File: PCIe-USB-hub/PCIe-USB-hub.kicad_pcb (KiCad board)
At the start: 4 copper layers, 135 parts, among them J2 USB3_A_Stacked, J3 USB3_A_Stacked, J4 USB3_A_Stacked, J5 USB3_A_Stacked, J6 USB3_A_Stacked, J7 Barrel_Jack_MountingPin, U1 ST1S10PUR, Y1 X322524MQB4SI, Y2 X322524MQB4SI, Y3 X322524MQB4SI

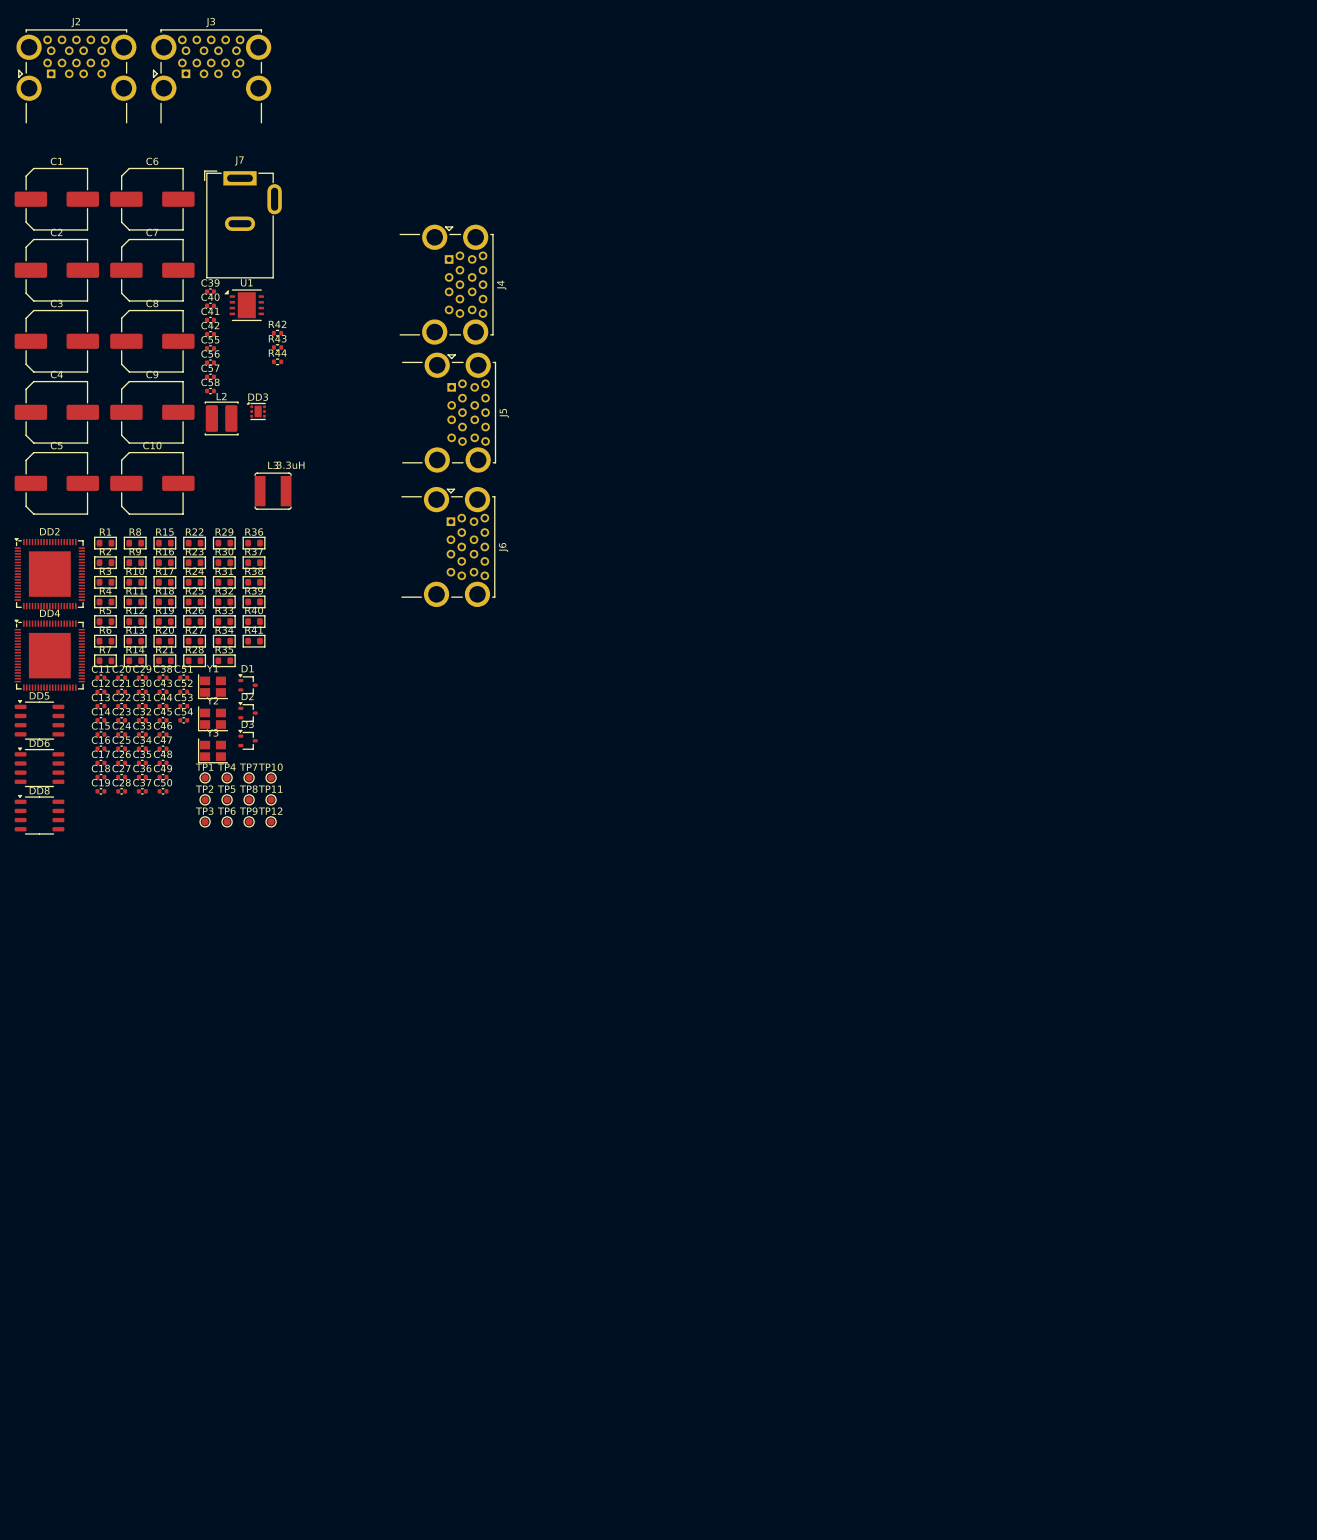
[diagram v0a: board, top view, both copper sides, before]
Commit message: Доделал схему, сделал контур платы и расстановку предварительную USB портов
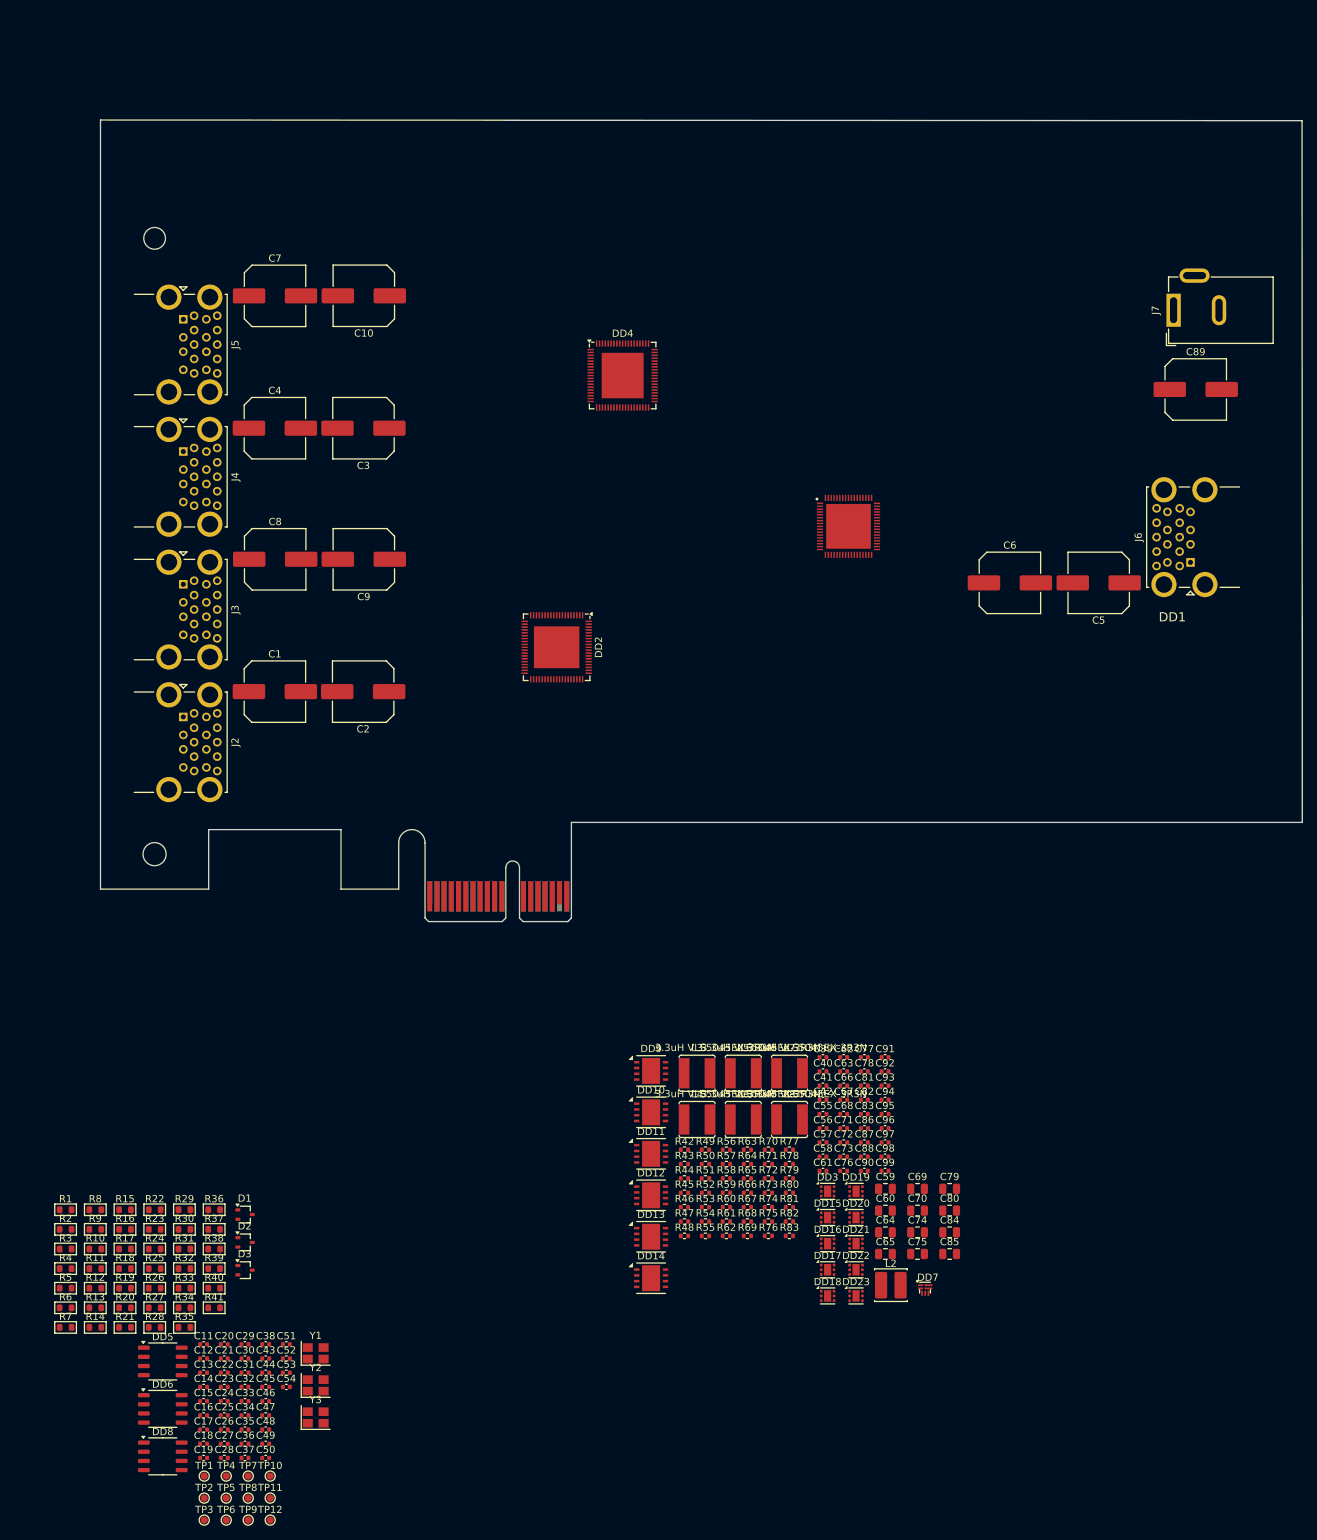
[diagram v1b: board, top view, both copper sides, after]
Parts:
- removed U1: ST1S10PUR, Package_DFN_QFN:DFN-8-1EP_4x4mm_P0.8mm_EP2.5x3.6mm
- added C59: 22uF, Capacitor_SMD:C_0805_2012Metric, F.Cu at (140.2, 175.3)
- added C60: 22uF, Capacitor_SMD:C_0805_2012Metric, F.Cu at (140.2, 178.3)
- added C61: 22uF, Capacitor_SMD:C_0402_1005Metric, F.Cu at (131.6, 172.8)
- added C62: 100nF, Capacitor_SMD:C_0402_1005Metric, F.Cu at (134.4, 157.1)
- added C63: 22uF, Capacitor_SMD:C_0402_1005Metric, F.Cu at (134.4, 159.1)
- added C64: 22uF, Capacitor_SMD:C_0805_2012Metric, F.Cu at (140.2, 181.4)
- added C65: 22uF, Capacitor_SMD:C_0805_2012Metric, F.Cu at (140.2, 184.4)
- added C66: 22uF, Capacitor_SMD:C_0402_1005Metric, F.Cu at (134.4, 161.0)
- added C67: 100nF, Capacitor_SMD:C_0402_1005Metric, F.Cu at (134.4, 163.0)
- added C68: 22uF, Capacitor_SMD:C_0402_1005Metric, F.Cu at (134.4, 165.0)
- added C69: 22uF, Capacitor_SMD:C_0805_2012Metric, F.Cu at (144.7, 175.3)
- added C70: 22uF, Capacitor_SMD:C_0805_2012Metric, F.Cu at (144.7, 178.3)
- added C71: 22uF, Capacitor_SMD:C_0402_1005Metric, F.Cu at (134.4, 166.9)
- added C72: 100nF, Capacitor_SMD:C_0402_1005Metric, F.Cu at (134.4, 168.9)
- added C73: 22uF, Capacitor_SMD:C_0402_1005Metric, F.Cu at (134.4, 170.9)
- added C74: 22uF, Capacitor_SMD:C_0805_2012Metric, F.Cu at (144.7, 181.4)
- added C75: 22uF, Capacitor_SMD:C_0805_2012Metric, F.Cu at (144.7, 184.4)
- added C76: 22uF, Capacitor_SMD:C_0402_1005Metric, F.Cu at (134.4, 172.8)
- added C77: 100nF, Capacitor_SMD:C_0402_1005Metric, F.Cu at (137.3, 157.1)
- added C78: 22uF, Capacitor_SMD:C_0402_1005Metric, F.Cu at (137.3, 159.1)
- added C79: 22uF, Capacitor_SMD:C_0805_2012Metric, F.Cu at (149.1, 175.3)
- added C80: 22uF, Capacitor_SMD:C_0805_2012Metric, F.Cu at (149.1, 178.3)
- added C81: 22uF, Capacitor_SMD:C_0402_1005Metric, F.Cu at (137.3, 161.0)
- added C82: 100nF, Capacitor_SMD:C_0402_1005Metric, F.Cu at (137.3, 163.0)
- added C83: 22uF, Capacitor_SMD:C_0402_1005Metric, F.Cu at (137.3, 165.0)
- added C84: 22uF, Capacitor_SMD:C_0805_2012Metric, F.Cu at (149.1, 181.4)
- added C85: 22uF, Capacitor_SMD:C_0805_2012Metric, F.Cu at (149.1, 184.4)
- added C86: 22uF, Capacitor_SMD:C_0402_1005Metric, F.Cu at (137.3, 166.9)
- added C87: 100nF, Capacitor_SMD:C_0402_1005Metric, F.Cu at (137.3, 168.9)
- added C88: 22uF, Capacitor_SMD:C_0402_1005Metric, F.Cu at (137.3, 170.9)
- added C89: EEEFK1E151P, Capacitor_SMD:C_Elec_8x10.2, F.Cu at (183.3, 64.5)
- added C90: 100nF, Capacitor_SMD:C_0402_1005Metric, F.Cu at (137.3, 172.8)
- added C91: 100nF, Capacitor_SMD:C_0402_1005Metric, F.Cu at (140.2, 157.1)
- added C92: 100nF, Capacitor_SMD:C_0402_1005Metric, F.Cu at (140.2, 159.1)
- added C93: 100nF, Capacitor_SMD:C_0402_1005Metric, F.Cu at (140.2, 161.0)
- added C94: 100nF, Capacitor_SMD:C_0402_1005Metric, F.Cu at (140.2, 163.0)
- added C95: 100nF, Capacitor_SMD:C_0402_1005Metric, F.Cu at (140.2, 165.0)
- added C96: 100nF, Capacitor_SMD:C_0402_1005Metric, F.Cu at (140.2, 166.9)
- added C97: 100nF, Capacitor_SMD:C_0402_1005Metric, F.Cu at (140.2, 168.9)
- added C98: 100nF, Capacitor_SMD:C_0402_1005Metric, F.Cu at (140.2, 170.9)
- added C99: 100nF, Capacitor_SMD:C_0402_1005Metric, F.Cu at (140.2, 172.8)
- added DD1: UPD720201K8-701-BAC-A, UPD720201K8:UPD720201K8, F.Cu at (135.1, 83.5)
- added DD10: ST1S10PUR, Package_DFN_QFN:DFN-8-1EP_4x4mm_P0.8mm_EP2.5x3.6mm, F.Cu at (107.7, 164.7)
- added DD11: ST1S10PUR, Package_DFN_QFN:DFN-8-1EP_4x4mm_P0.8mm_EP2.5x3.6mm, F.Cu at (107.7, 170.5)
- added DD12: ST1S10PUR, Package_DFN_QFN:DFN-8-1EP_4x4mm_P0.8mm_EP2.5x3.6mm, F.Cu at (107.7, 176.2)
- added DD13: ST1S10PUR, Package_DFN_QFN:DFN-8-1EP_4x4mm_P0.8mm_EP2.5x3.6mm, F.Cu at (107.7, 182.0)
- added DD14: ST1S10PUR, Package_DFN_QFN:DFN-8-1EP_4x4mm_P0.8mm_EP2.5x3.6mm, F.Cu at (107.7, 187.7)
- added DD15: TPS2552DRVR, Package_SON:WSON-6-1EP_2x2mm_P0.65mm_EP1x1.6mm, F.Cu at (132.2, 179.3)
- added DD16: TPS2552DRVR, Package_SON:WSON-6-1EP_2x2mm_P0.65mm_EP1x1.6mm, F.Cu at (132.2, 182.9)
- added DD17: TPS2552DRVR, Package_SON:WSON-6-1EP_2x2mm_P0.65mm_EP1x1.6mm, F.Cu at (132.2, 186.6)
- added DD18: TPS2552DRVR, Package_SON:WSON-6-1EP_2x2mm_P0.65mm_EP1x1.6mm, F.Cu at (132.2, 190.2)
- added DD19: TPS2552DRVR, Package_SON:WSON-6-1EP_2x2mm_P0.65mm_EP1x1.6mm, F.Cu at (136.2, 175.7)
- added DD20: TPS2552DRVR, Package_SON:WSON-6-1EP_2x2mm_P0.65mm_EP1x1.6mm, F.Cu at (136.2, 179.3)
- added DD21: TPS2552DRVR, Package_SON:WSON-6-1EP_2x2mm_P0.65mm_EP1x1.6mm, F.Cu at (136.2, 182.9)
- added DD22: TPS2552DRVR, Package_SON:WSON-6-1EP_2x2mm_P0.65mm_EP1x1.6mm, F.Cu at (136.2, 186.6)
- added DD23: TPS2552DRVR, Package_SON:WSON-6-1EP_2x2mm_P0.65mm_EP1x1.6mm, F.Cu at (136.2, 190.2)
- added DD7: ~, SY8843QWC:SY8843QWC, F.Cu at (145.6, 186.6)
- added DD9: ST1S10PUR, Package_DFN_QFN:DFN-8-1EP_4x4mm_P0.8mm_EP2.5x3.6mm, F.Cu at (107.7, 159.0)
- added J1: PCIexpress_x1, PCIexpress:PCIexpress_x1, F.Cu at (76.5, 138.3)
- added L4: 3.3uH VLS5045EX-3R3N, PCM_4ms_Inductor:COIL_5040, F.Cu at (114.1, 165.7)
- added L5: 3.3uH VLS5045EX-3R3N, PCM_4ms_Inductor:COIL_5040, F.Cu at (120.5, 159.3)
- added L6: 3.3uH VLS5045EX-3R3N, PCM_4ms_Inductor:COIL_5040, F.Cu at (120.5, 165.7)
- added L7: 3.3uH VLS5045EX-3R3N, PCM_4ms_Inductor:COIL_5040, F.Cu at (126.9, 159.3)
- added L8: 3.3uH VLS5045EX-3R3N, PCM_4ms_Inductor:COIL_5040, F.Cu at (126.9, 165.7)
- added R45: 0R, Resistor_SMD:R_0402_1005Metric, F.Cu at (112.4, 175.9)
- added R46: 0R, Resistor_SMD:R_0402_1005Metric, F.Cu at (112.4, 177.9)
- added R47: 4.7k, Resistor_SMD:R_0402_1005Metric, F.Cu at (112.4, 179.9)
- added R48: 1.5k, Resistor_SMD:R_0402_1005Metric, F.Cu at (112.4, 181.9)
- added R49: 0R, Resistor_SMD:R_0402_1005Metric, F.Cu at (115.3, 169.9)
- added R50: 43k, Resistor_SMD:R_0402_1005Metric, F.Cu at (115.3, 171.9)
- added R51: 8.2k, Resistor_SMD:R_0402_1005Metric, F.Cu at (115.3, 173.9)
- added R52: 0R, Resistor_SMD:R_0402_1005Metric, F.Cu at (115.3, 175.9)
- added R53: 43k, Resistor_SMD:R_0402_1005Metric, F.Cu at (115.3, 177.9)
- added R54: 8.2k, Resistor_SMD:R_0402_1005Metric, F.Cu at (115.3, 179.9)
- added R55: 0R, Resistor_SMD:R_0402_1005Metric, F.Cu at (115.3, 181.9)
- added R56: 43k, Resistor_SMD:R_0402_1005Metric, F.Cu at (118.2, 169.9)
- added R57: 8.2k, Resistor_SMD:R_0402_1005Metric, F.Cu at (118.2, 171.9)
- added R58: 0R, Resistor_SMD:R_0402_1005Metric, F.Cu at (118.2, 173.9)
- added R59: 43k, Resistor_SMD:R_0402_1005Metric, F.Cu at (118.2, 175.9)
- added R60: 8.2k, Resistor_SMD:R_0402_1005Metric, F.Cu at (118.2, 177.9)
- added R61: 0R, Resistor_SMD:R_0402_1005Metric, F.Cu at (118.2, 179.9)
- added R62: 43k, Resistor_SMD:R_0402_1005Metric, F.Cu at (118.2, 181.9)
- added R63: 8.2k, Resistor_SMD:R_0402_1005Metric, F.Cu at (121.1, 169.9)
- added R64: 100k, Resistor_SMD:R_0402_1005Metric, F.Cu at (121.1, 171.9)
- added R65: 20k, Resistor_SMD:R_0402_1005Metric, F.Cu at (121.1, 173.9)
- added R66: 100k, Resistor_SMD:R_0402_1005Metric, F.Cu at (121.1, 175.9)
- added R67: 20k, Resistor_SMD:R_0402_1005Metric, F.Cu at (121.1, 177.9)
- added R68: 100k, Resistor_SMD:R_0402_1005Metric, F.Cu at (121.1, 179.9)
- added R69: 100k, Resistor_SMD:R_0402_1005Metric, F.Cu at (121.1, 181.9)
- added R70: 20k, Resistor_SMD:R_0402_1005Metric, F.Cu at (124.0, 169.9)
- added R71: 20k, Resistor_SMD:R_0402_1005Metric, F.Cu at (124.0, 171.9)
- added R72: 100k, Resistor_SMD:R_0402_1005Metric, F.Cu at (124.0, 173.9)
- added R73: 100k, Resistor_SMD:R_0402_1005Metric, F.Cu at (124.0, 175.9)
- added R74: 20k, Resistor_SMD:R_0402_1005Metric, F.Cu at (124.0, 177.9)
- added R75: 20k, Resistor_SMD:R_0402_1005Metric, F.Cu at (124.0, 179.9)
- added R76: 100k, Resistor_SMD:R_0402_1005Metric, F.Cu at (124.0, 181.9)
- added R77: 100k, Resistor_SMD:R_0402_1005Metric, F.Cu at (126.9, 169.9)
- added R78: 20k, Resistor_SMD:R_0402_1005Metric, F.Cu at (126.9, 171.9)
- added R79: 20k, Resistor_SMD:R_0402_1005Metric, F.Cu at (126.9, 173.9)
- added R80: 100k, Resistor_SMD:R_0402_1005Metric, F.Cu at (126.9, 175.9)
- added R81: 100k, Resistor_SMD:R_0402_1005Metric, F.Cu at (126.9, 177.9)
- added R82: 20k, Resistor_SMD:R_0402_1005Metric, F.Cu at (126.9, 179.9)
- added R83: 20k, Resistor_SMD:R_0402_1005Metric, F.Cu at (126.9, 181.9)
- L3: value 3.3uH -> 3.3uH VLS5045EX-3R3N
- R43: value 14k -> 51.1k
- R44: value 24k -> 68k
- moved L2 151.8 mm to (141.0, 188.7)
- moved C5 145.1 mm to (169.8, 91.3), turned to 180 degrees
- moved C39 136.0 mm to (131.6, 157.1)
- moved C40 136.0 mm to (131.6, 159.1)
- moved C41 136.0 mm to (131.6, 161.0)
- moved C42 136.0 mm to (131.6, 163.0)
- moved C55 136.0 mm to (131.6, 165.0)
- moved C56 136.0 mm to (131.6, 166.9)
- moved C57 136.0 mm to (131.6, 168.9)
- moved C58 136.0 mm to (131.6, 170.9)
- moved DD3 133.9 mm to (132.2, 175.7)
- moved J7 130.7 mm to (180.2, 53.5), turned to 90 degrees
- moved C6 130.3 mm to (157.5, 91.3)
- moved R44 126.5 mm to (112.4, 173.9)
- moved R43 126.5 mm to (112.4, 171.9)
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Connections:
- net 0.95V renamed 1.05V
- DD2 pad 55: OCI2B -> OCI1B
- DD2 pad 59: OCI4B -> OCI3B
- DD3 pad 1: unconnected-(DD3-OUT-Pad1) -> +5V_USB1
- DD3 pad 2: unconnected-(DD3-ILIM-Pad2) -> Net-(DD3-ILIM)
- DD3 pad 3: unconnected-(DD3-#FAULT-Pad3) -> Net-(DD3-#FAULT)
- DD3 pad 5: unconnected-(DD3-GND-Pad5) -> Earth
- DD3 pad 6: unconnected-(DD3-EN-Pad6) -> OCI1B
- DD3 pad 7: unconnected-(DD3-EP-Pad7) -> Earth
- DD4 pad 55: OCI6B -> OCI5B
- DD4 pad 59: OCI8B -> OCI7B
- J7 pad 1: unconnected-(J7-Pad1) -> +12V
- J7 pad 2: unconnected-(J7-Pad2) -> Earth
- L3 pad 1: unconnected-(L3-Pad1) -> Net-(DD9-SW)
- L3 pad 2: unconnected-(L3-Pad2) -> +3.3V_DUAL
- R22 pad 1: OCI9B -> OCI10B
- R27 pad 2: OCI2B -> OCI1B
- R29 pad 2: OCI4B -> OCI3B
- R35 pad 2: OCI6B -> OCI5B
- R37 pad 2: OCI8B -> OCI7B
- R42 pad 1: POW_95_EN -> +3.3V
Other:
- board outline added: 166.7 x 111.2 mm

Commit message: тык тык поменял разъёмы на одинарные
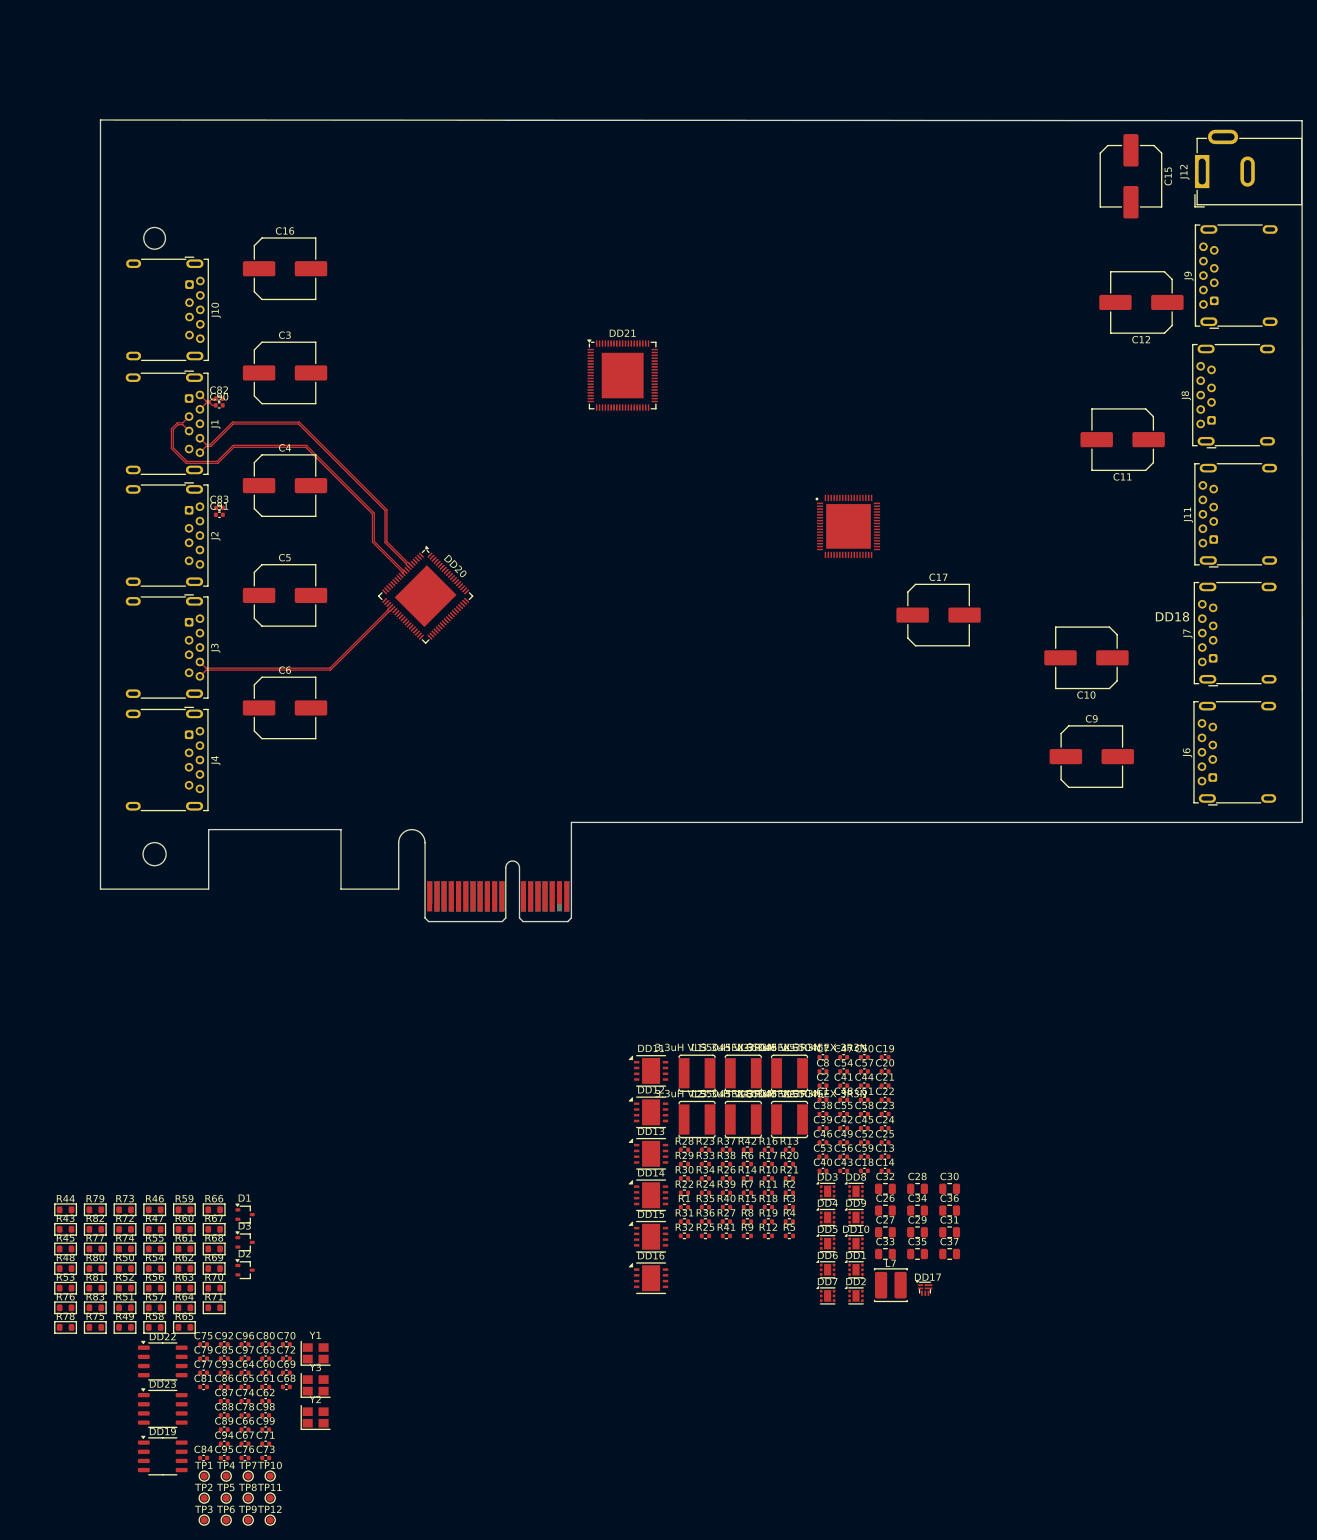
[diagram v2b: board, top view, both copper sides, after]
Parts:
- removed the J5 at (42.9, 54.8)
- added J1: USB3_A, Connector_USB:USB3_A_Molex_48393-001, F.Cu at (43.7, 65.8)
- added J10: USB3_A, Connector_USB:USB3_A_Molex_48393-001, F.Cu at (43.7, 50.0)
- added J11: USB3_A, Connector_USB:USB3_A_Molex_48393-001, F.Cu at (185.8, 85.3)
- added J7: USB3_A, Connector_USB:USB3_A_Molex_48393-001, F.Cu at (185.7, 101.8)
- added J8: USB3_A, Connector_USB:USB3_A_Molex_48393-001, F.Cu at (185.4, 68.8)
- added J9: USB3_A, Connector_USB:USB3_A_Molex_48393-001, F.Cu at (185.8, 52.2)
- J2, J3, J4, J6: value USB3_A_Stacked -> USB3_A; footprint Connector_USB:USB3_A_Molex_48406-0001_Horizontal_Stacked -> Connector_USB:USB3_A_Molex_48393-001
- moved C82 141.0 mm to (47.9, 65.8)
- moved C90 138.1 mm to (47.9, 66.7)
- moved C91 128.8 mm to (47.9, 81.9)
- moved C83 127.8 mm to (47.9, 80.9)
- moved C9 122.1 mm to (168.8, 115.4)
- moved C16 120.9 mm to (57.0, 47.8), turned to 0 degrees
- moved C11 119.2 mm to (173.1, 71.5), turned to 180 degrees
- moved C12 107.8 mm to (175.7, 52.4)
- moved C10 105.2 mm to (168.1, 101.7)
- moved C3 44.2 mm to (57.0, 62.2)
- moved J4 39.3 mm to (43.7, 112.4)
- moved C15 30.9 mm to (174.3, 34.9), turned to -90 degrees
- moved C4 30.6 mm to (57.0, 77.8), turned to 0 degrees
- moved J6 30.0 mm to (185.6, 118.3)
- moved J2 28.7 mm to (43.7, 81.2)
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- renumbered C42 to C1, C3 to C10, C7 to C11, C10 to C12, C98 to C13, C99 to C14, C89 to C15, C5 to C16, C6 to C17, C90 to C18, C91 to C19, C41 to C2, C92 to C20, C93 to C21, C94 to C22, C95 to C23, C96 to C24, C97 to C25, C60 to C26, C64 to C27, C69 to C28, C74 to C29, C1 to C3, C79 to C30, C84 to C31, C59 to C32, C65 to C33, C70 to C34, C75 to C35, C80 to C36, C85 to C37, C55 to C38, C56 to C39, C2 to C4, C61 to C40, C66 to C41, C71 to C42, C76 to C43, C81 to C44, C86 to C45, C57 to C46, C62 to C47, C67 to C48, C72 to C49, C8 to C5, C77 to C50, C82 to C51, C87 to C52, C58 to C53, C63 to C54, C68 to C55, C73 to C56, C78 to C57, C83 to C58, C88 to C59, C9 to C6, C44 to C60, C45 to C61, C46 to C62, C43 to C63, C31 to C64, C32 to C65, C35 to C66, C36 to C67, C54 to C68, C53 to C69, C39 to C7, C51 to C70, C49 to C71, C52 to C72, C50 to C73, C33 to C74, C11 to C75, C37 to C76, C13 to C77, C34 to C78, C12 to C79, C40 to C8, C38 to C80, C14 to C81, C16 to C82, C17 to C83, C19 to C84, C21 to C85, C23 to C86, C24 to C87, C25 to C88, C26 to C89, C4 to C9, C15 to C90, C18 to C91, C20 to C92, C22 to C93, C27 to C94, C28 to C95, C29 to C96, C30 to C97, C47 to C98, C48 to C99, D3 to D2, D2 to D3, DD22 to DD1, DD21 to DD10, DD9 to DD11, DD10 to DD12, DD11 to DD13, DD12 to DD14, DD13 to DD15, DD14 to DD16, DD7 to DD17, DD1 to DD18, DD8 to DD19, DD23 to DD2, DD2 to DD20, DD4 to DD21, DD5 to DD22, DD6 to DD23, DD15 to DD4, DD16 to DD5, DD17 to DD6, DD18 to DD7, DD19 to DD8, DD20 to DD9, J7 to J12, J1 to J5, L3 to L1, L4 to L2, L5 to L3, L6 to L4, L7 to L5, L8 to L6, L2 to L7, R46 to R1, R72 to R10, R73 to R11, R76 to R12, R77 to R13, R65 to R14, R67 to R15, R70 to R16, R71 to R17, R74 to R18, R75 to R19, R80 to R2, R78 to R20, R79 to R21, R45 to R22, R49 to R23, R52 to R24, R55 to R25, R58 to R26, R61 to R27, R42 to R28, R43 to R29, R81 to R3, R44 to R30, R47 to R31, R48 to R32, R50 to R33, R51 to R34, R53 to R35, R54 to R36, R56 to R37, R57 to R38, R59 to R39, R82 to R4, R60 to R40, R62 to R41, R63 to R42, R2 to R43, R1 to R44, R3 to R45, R22 to R46, R23 to R47, R4 to R48, R21 to R49, R83 to R5, R18 to R50, R20 to R51, R19 to R52, R5 to R53, R25 to R54, R24 to R55, R26 to R56, R27 to R57, R28 to R58, R29 to R59, R64 to R6, R30 to R60, R31 to R61, R32 to R62, R33 to R63, R34 to R64, R35 to R65, R36 to R66, R37 to R67, R38 to R68, R39 to R69, R66 to R7, R40 to R70, R41 to R71, R16 to R72, R15 to R73, R17 to R74, R14 to R75, R6 to R76, R10 to R77, R7 to R78, R8 to R79, R68 to R8, R11 to R80, R12 to R81, R9 to R82, R13 to R83, R69 to R9, Y3 to Y2, Y2 to Y3
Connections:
- DD1 pad 4: (no net) -> PPON9
- DD10 pad 4: (no net) -> PPON8
- DD2 pad 4: (no net) -> PPON10
- DD3 pad 4: (no net) -> PPON1
- DD4 pad 4: (no net) -> PPON2
- DD5 pad 4: (no net) -> PPON3
- DD6 pad 4: (no net) -> PPON4
- DD7 pad 4: (no net) -> PPON5
- DD8 pad 4: (no net) -> PPON6
- DD9 pad 4: (no net) -> PPON7
- J2 pad 1: +5V_USB1 -> +5V_USB2
- J2 pad 10: +5V_USB2 -> Earth
- J2 pad 2: USB-downstream1-D- -> USB-downstream2-D-
- J2 pad 3: USB-downstream1-D+ -> USB-downstream2-D+
- J2 pad 5: USB-downstream1-RX- -> USB-downstream2-RX-
- J2 pad 6: USB-downstream1-RX+ -> USB-downstream2-RX+
- J2 pad 8: USB-downstream1-TX- -> USB-downstream2-TX-
- J2 pad 9: USB-downstream1-TX+ -> USB-downstream2-TX+
- J3 pad 10: +5V_USB4 -> Earth
- J4 pad 1: +5V_USB5 -> +5V_USB4
- J4 pad 10: +5V_USB6 -> Earth
- J4 pad 2: USB-downstream5-D- -> USB-downstream4-D-
- J4 pad 3: USB-downstream5-D+ -> USB-downstream4-D+
- J4 pad 5: USB-downstream5-RX- -> USB-downstream4-RX-
- J4 pad 6: USB-downstream5-RX+ -> USB-downstream4-RX+
- J4 pad 8: USB-downstream5-TX- -> USB-downstream4-TX-
- J4 pad 9: USB-downstream5-TX+ -> USB-downstream4-TX+
- J6 pad 1: +5V_USB9 -> +5V_USB5
- J6 pad 10: +5V_USB10 -> Earth
- J6 pad 2: USB-downstream9-D- -> USB-downstream5-D-
- J6 pad 3: USB-downstream9-D+ -> USB-downstream5-D+
- J6 pad 5: USB-downstream9-RX- -> USB-downstream5-RX-
- J6 pad 6: USB-downstream9-RX+ -> USB-downstream5-RX+
- J6 pad 8: USB-downstream9-TX- -> USB-downstream5-TX-
- J6 pad 9: USB-downstream9-TX+ -> USB-downstream5-TX+
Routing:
- net USB-downstream1-D-: track 0.00 -> 49.4 mm
- net USB-downstream1-D+: track 0.00 -> 48.7 mm
- net USB-downstream1-RX+: track 0.00 -> 41.8 mm
- net USB-downstream1-RX-: track 0.00 -> 41.6 mm
- net USB-downstream3-RX-: track 0.00 -> 30.6 mm
- net USB-downstream3-RX+: track 0.00 -> 30.4 mm
- net USB-downstream1-TX-: track 0.00 -> 2.70 mm
- net USB-downstream1-TX+: track 0.00 -> 2.70 mm
